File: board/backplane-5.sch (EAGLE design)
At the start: 143 parts, among them CN1 RJ45JACK90, U1 AMS1117-5.0, U10 RT9193, U11 KSZ9897, U12 KSZ8081MLX, U13 STM32F217-100, U2 AMS1117-5.0, U3 AMS1117-5.0, U4 AMS1117-5.0, U5 AMS1117-5.0, U6 AMS1117-2.5, U7 AMS1117-1.2, U8 RT9193, U9 AMS1117-5.0, X1 25MHz, X2 25MHz

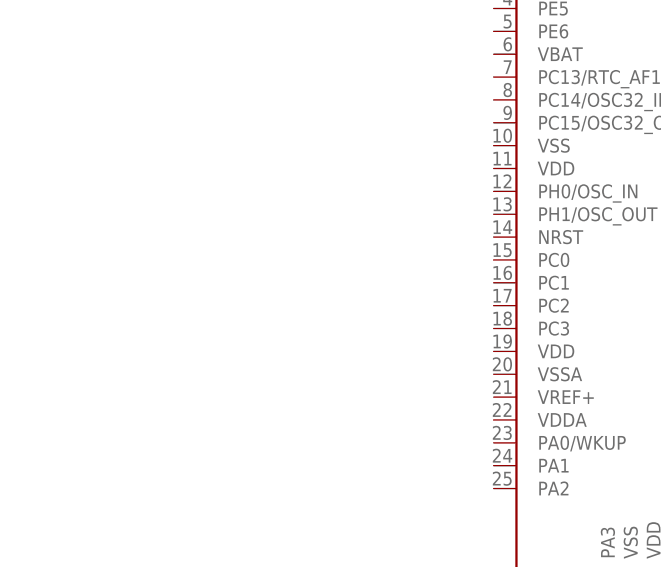
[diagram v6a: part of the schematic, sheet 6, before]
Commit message: Added STM Crystal and fixed some devices
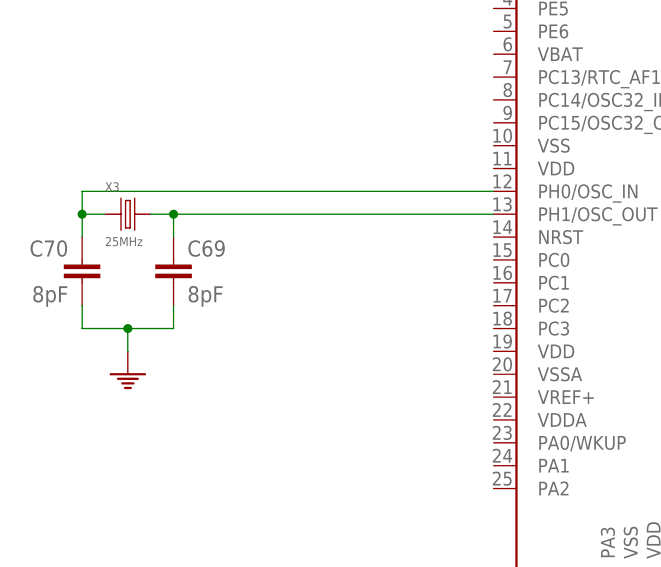
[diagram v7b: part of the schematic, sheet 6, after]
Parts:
- added C69, C70: 8pF, tuetuopay:C0603
- added X3: 25MHz, tuetuopay:CRYSTAL
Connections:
- new net N$21: C69.1, U13.PH1/OSC_OUT, X3.P$1
- new net N$22: C70.1, U13.PH0/OSC_IN, X3.P$2
- net GND: now also C69.2, C70.2
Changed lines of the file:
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@@
 <part name="FRAME6" library="frames" library_urn="urn:adsk.eagle:library:229" deviceset="A4L-LOC" device=""/>
 <part name="U13" library="tuetuopay" deviceset="STM32F217-100" device=""/>
+<part name="X3" library="tuetuopay" deviceset="CRYSTAL" device="" value="25MHz"/>
+<part name="C69" library="tuetuopay" deviceset="C" device="0603" value="8pF"/>
+<part name="C70" library="tuetuopay" deviceset="C" device="0603" value="8pF"/>
+<part name="PE28" library="supply1" library_urn="urn:adsk.eagle:library:371" deviceset="PE" device=""/>
 </parts>
 <sheets>
@@
 <instance part="FRAME6" gate="G$1" x="0" y="0"/>
 <instance part="U13" gate="G$1" x="109.22" y="91.44"/>
+<instance part="X3" gate="G$1" x="22.86" y="93.98"/>
+<instance part="C69" gate="&gt;NAME" x="27.94" y="88.9"/>
+<instance part="C70" gate="&gt;NAME" x="17.78" y="88.9" rot="MR0"/>
+<instance part="PE28" gate="M" x="22.86" y="76.2" smashed="yes"/>
 </instances>
 <busses>
 </busses>
 <nets>
+<net name="GND" class="0">
+<segment>
+<pinref part="C70" gate="&gt;NAME" pin="2"/>
+<wire x1="17.78" y1="83.82" x2="17.78" y2="81.28" width="0.1524" layer="91"/>
+<pinref part="C69" gate="&gt;NAME" pin="2"/>
+<wire x1="17.78" y1="81.28" x2="22.86" y2="81.28" width="0.1524" layer="91"/>
+<wire x1="22.86" y1="81.28" x2="27.94" y2="81.28" width="0.1524" layer="91"/>
+<wire x1="27.94" y1="81.28" x2="27.94" y2="83.82" width="0.1524" layer="91"/>
+<pinref part="PE28" gate="M" pin="PE"/>
+<wire x1="22.86" y1="81.28" x2="22.86" y2="78.74" width="0.1524" layer="91"/>
+<junction x="22.86" y="81.28"/>
+</segment>
+</net>
+<net name="N$21" class="0">
+<segment>
+<pinref part="X3" gate="G$1" pin="P$1"/>
+<pinref part="U13" gate="G$1" pin="PH1/OSC_OUT"/>
+<wire x1="25.4" y1="93.98" x2="27.94" y2="93.98" width="0.1524" layer="91"/>
+<pinref part="C69" gate="&gt;NAME" pin="1"/>
+<wire x1="27.94" y1="93.98" x2="63.5" y2="93.98" width="0.1524" layer="91"/>
+<wire x1="27.94" y1="91.44" x2="27.94" y2="93.98" width="0.1524" layer="91"/>
+<junction x="27.94" y="93.98"/>
+</segment>
+</net>
+<net name="N$22" class="0">
+<segment>
+<pinref part="C70" gate="&gt;NAME" pin="1"/>
+<wire x1="17.78" y1="91.44" x2="17.78" y2="93.98" width="0.1524" layer="91"/>
+<pinref part="U13" gate="G$1" pin="PH0/OSC_IN"/>
+<wire x1="17.78" y1="93.98" x2="17.78" y2="96.52" width="0.1524" layer="91"/>
+<wire x1="17.78" y1="96.52" x2="63.5" y2="96.52" width="0.1524" layer="91"/>
+<pinref part="X3" gate="G$1" pin="P$2"/>
+<wire x1="20.32" y1="93.98" x2="17.78" y2="93.98" width="0.1524" layer="91"/>
+<junction x="17.78" y="93.98"/>
+</segment>
+</net>
 </nets>
 </sheet>

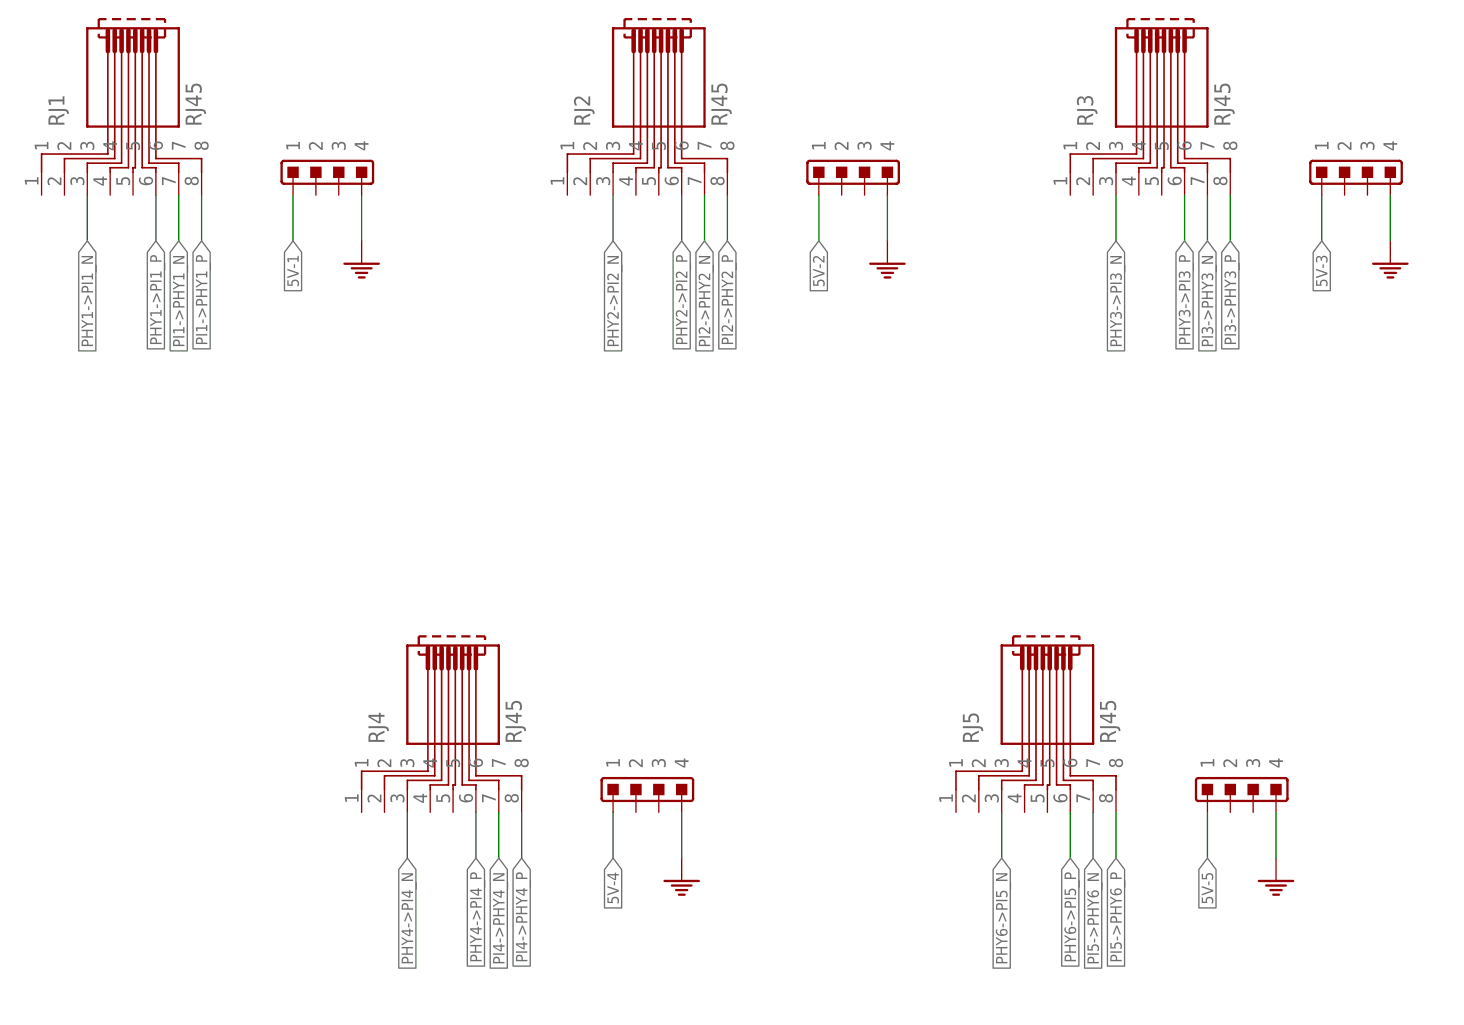
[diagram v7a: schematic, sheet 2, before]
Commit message: Fixed the naming of some components (incl. library)
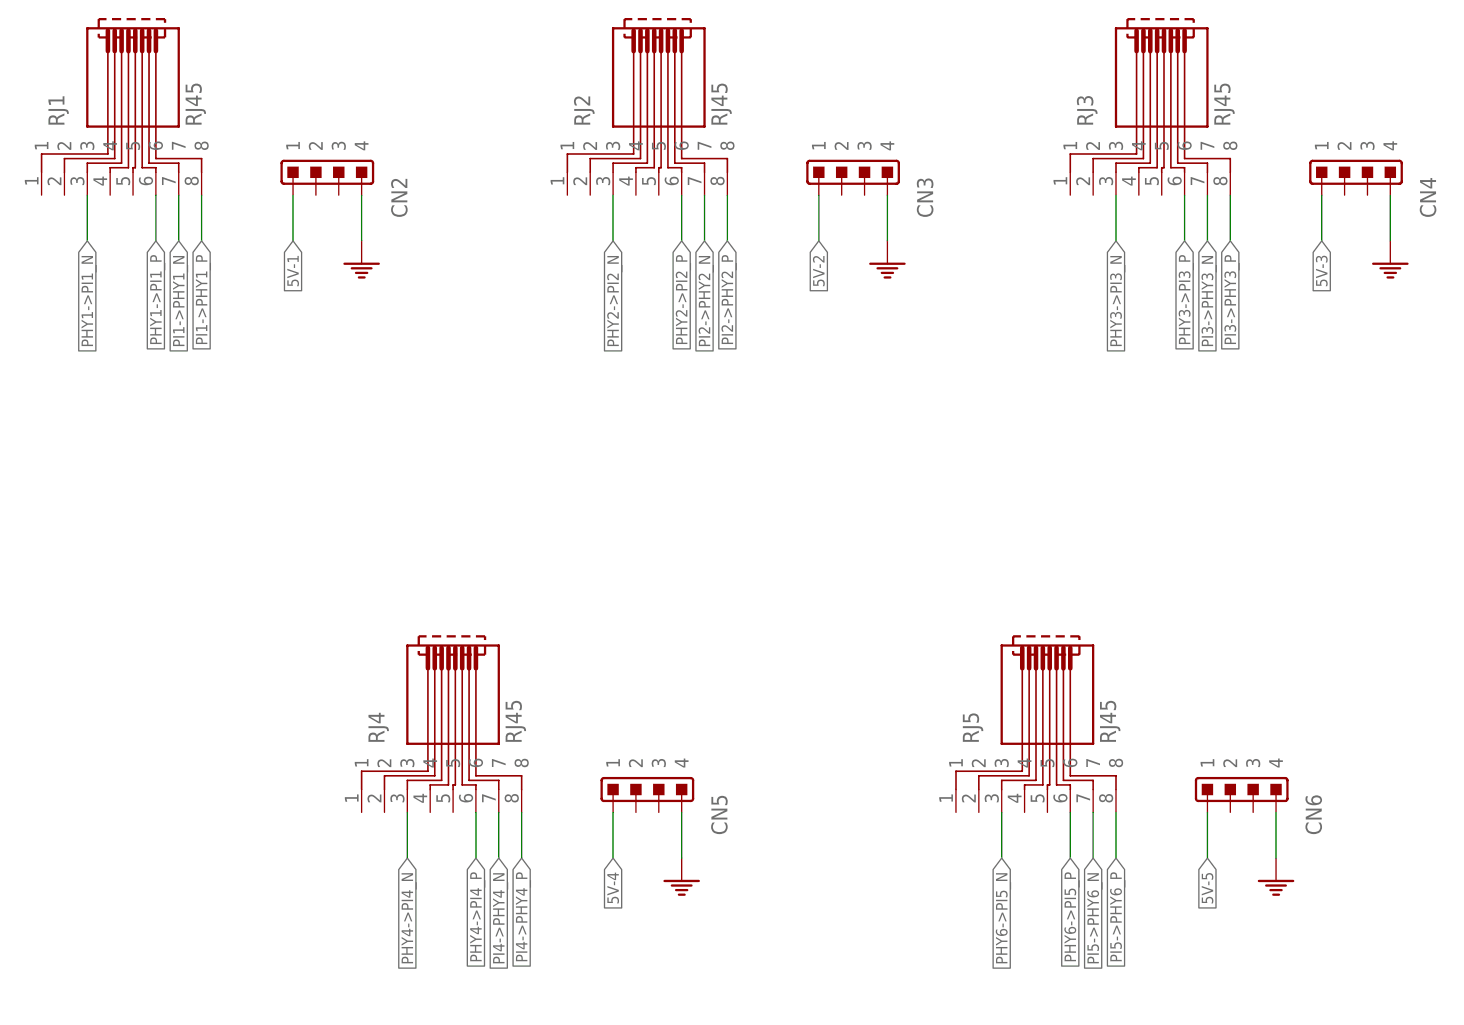
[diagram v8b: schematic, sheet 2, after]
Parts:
- renumbered U$1 to CN2, U$2 to CN3, U$3 to CN4, U$4 to CN5, U$5 to CN6, X1 to Y1, X2 to Y2, X3 to Y3
